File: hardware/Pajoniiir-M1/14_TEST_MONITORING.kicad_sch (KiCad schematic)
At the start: 12 parts, among them U14 INA238AIDGSR

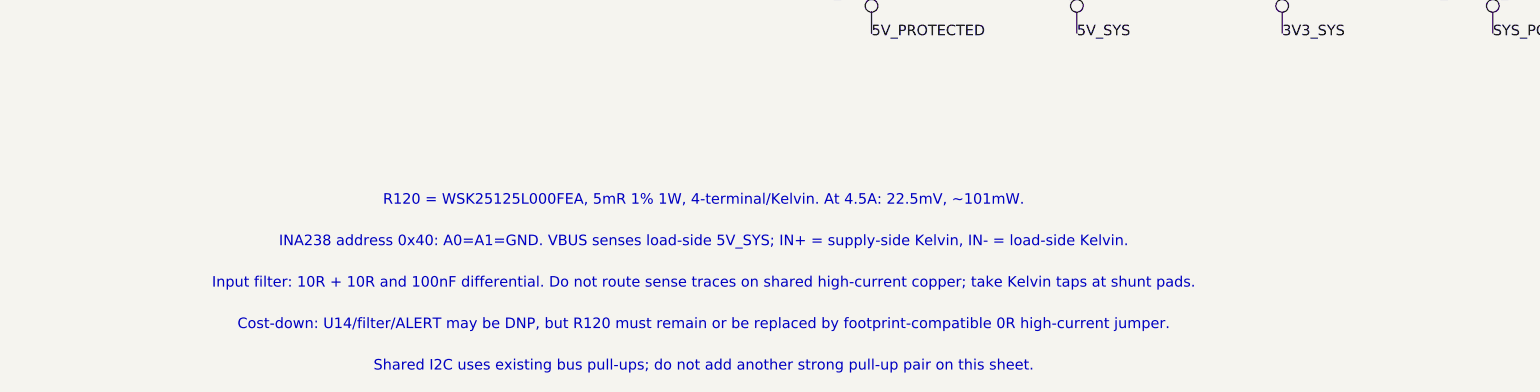
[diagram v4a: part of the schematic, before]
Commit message: hardware: constrain RefDes migration to annotation fields
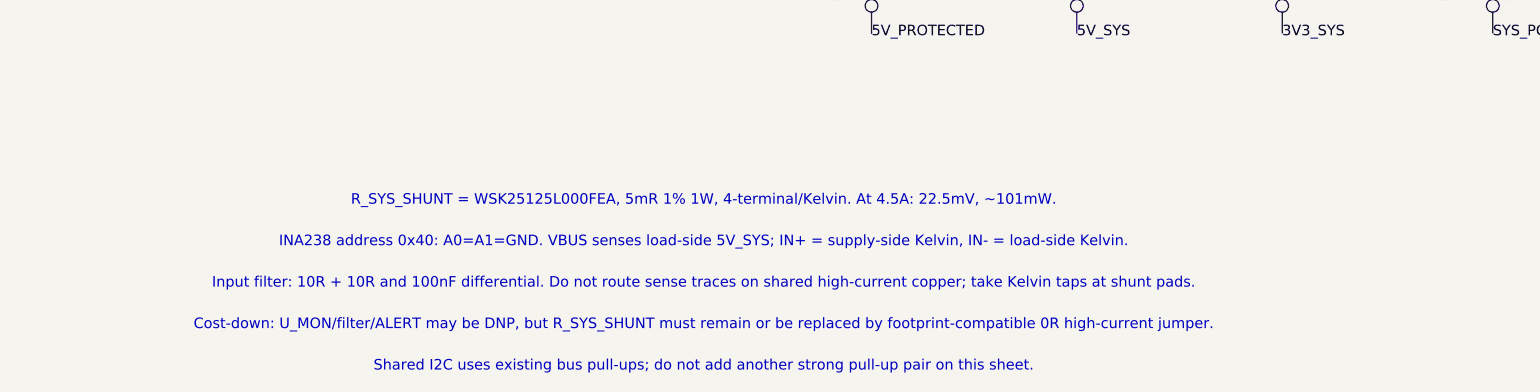
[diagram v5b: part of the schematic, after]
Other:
- note added: "Cost-down: U_MON/filter/ALERT may be DNP, but R_SYS_SHUNT must remain or be replaced by footprint-compatible 0R high-current jumper."
- note added: "R_SYS_SHUNT = WSK25125L000FEA, 5mR 1% 1W, 4-terminal/Kelvin. At 4.5A: 22.5mV, ~101mW."
- note removed: "Cost-down: U14/filter/ALERT may be DNP, but R120 must remain or be replaced by footprint-compatible 0R high-current jumper."
- note removed: "R120 = WSK25125L000FEA, 5mR 1% 1W, 4-terminal/Kelvin. At 4.5A: 22.5mV, ~101mW."
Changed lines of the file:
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@@
   )
   (label "SYS_POWER_ALERT_N" (at 130.175 104.775 0) (effects (font (size 1.27 1.27))))
-  (text "R120 = WSK25125L000FEA, 5mR 1% 1W, 4-terminal/Kelvin. At 4.5A: 22.5mV, ~101mW." (exclude_from_sim no) (at 35 125 0) (effects (font (size 1.27 1.27))))
+  (text "R_SYS_SHUNT = WSK25125L000FEA, 5mR 1% 1W, 4-terminal/Kelvin. At 4.5A: 22.5mV, ~101mW." (exclude_from_sim no) (at 35 125 0) (effects (font (size 1.27 1.27))))
   (text "INA238 address 0x40: A0=A1=GND. VBUS senses load-side 5V_SYS; IN+ = supply-side Kelvin, IN- = load-side Kelvin." (exclude_from_sim no) (at 35 130 0) (effects (font (size 1.27 1.27))))
   (text "Input filter: 10R + 10R and 100nF differential. Do not route sense traces on shared high-current copper; take Kelvin taps at shunt pads." (exclude_from_sim no) (at 35 135 0) (effects (font (size 1.27 1.27))))
-  (text "Cost-down: U14/filter/ALERT may be DNP, but R120 must remain or be replaced by footprint-compatible 0R high-current jumper." (exclude_from_sim no) (at 35 140 0) (effects (font (size 1.27 1.27))))
+  (text "Cost-down: U_MON/filter/ALERT may be DNP, but R_SYS_SHUNT must remain or be replaced by footprint-compatible 0R high-current jumper." (exclude_from_sim no) (at 35 140 0) (effects (font (size 1.27 1.27))))
   (text "Shared I2C uses existing bus pull-ups; do not add another strong pull-up pair on this sheet." (exclude_from_sim no) (at 35 145 0) (effects (font (size 1.27 1.27))))
   (sheet_instances (path "/" (page "15")))
